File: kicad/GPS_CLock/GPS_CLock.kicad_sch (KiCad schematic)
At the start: 40 parts, among them J101 SWD, J102 UART, SW101 BOOT_JMP, SW102 SW_Push, SW103 SW_Push, U101 W25Q16JVUXIQ, U102 VEML7700-TR, U103 RP2040, U104 MS8607

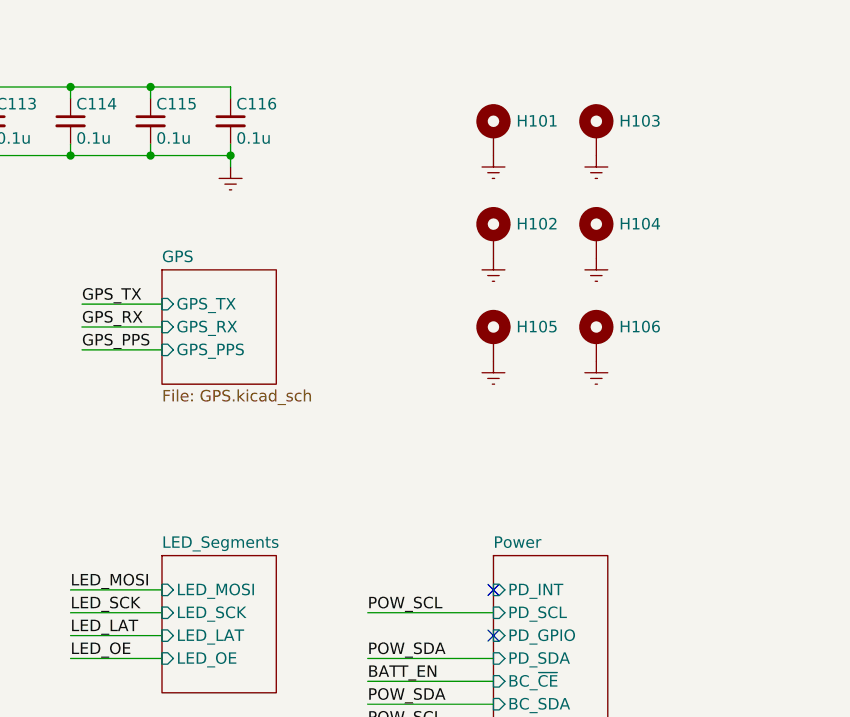
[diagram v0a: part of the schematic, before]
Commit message: change to larger segments
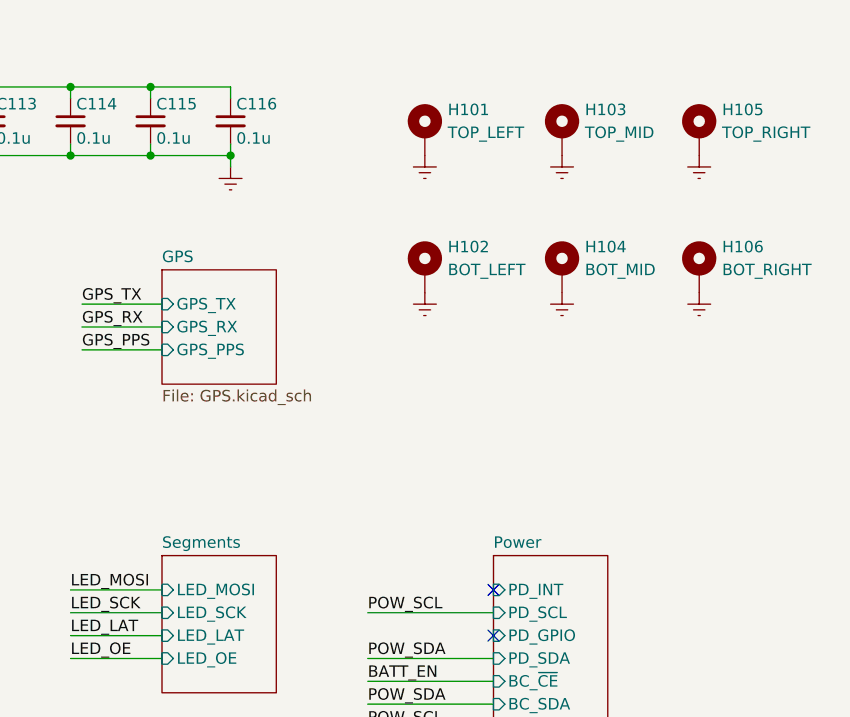
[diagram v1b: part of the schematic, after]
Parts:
- H101: value MountingHole_Pad -> TOP_LEFT; footprint MountingHole:MountingHole_2.2mm_M2_DIN965_Pad -> MountingHole:MountingHole_3.2mm_M3_DIN965_Pad
- H102: value MountingHole_Pad -> BOT_LEFT; footprint MountingHole:MountingHole_2.2mm_M2_DIN965_Pad -> MountingHole:MountingHole_3.2mm_M3_DIN965_Pad
- H103: value MountingHole_Pad -> TOP_MID; footprint MountingHole:MountingHole_2.2mm_M2_DIN965_Pad -> MountingHole:MountingHole_3.2mm_M3_DIN965_Pad
- H104: value MountingHole_Pad -> BOT_MID; footprint MountingHole:MountingHole_2.2mm_M2_DIN965_Pad -> MountingHole:MountingHole_3.2mm_M3_DIN965_Pad
- H105: value MountingHole_Pad -> TOP_RIGHT; footprint MountingHole:MountingHole_2.2mm_M2_DIN965_Pad -> MountingHole:MountingHole_3.2mm_M3_DIN965_Pad
- H106: value MountingHole_Pad -> BOT_RIGHT; footprint MountingHole:MountingHole_2.2mm_M2_DIN965_Pad -> MountingHole:MountingHole_3.2mm_M3_DIN965_Pad
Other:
- sheet LED_Segments renamed Segments
- sheet Segments: file LED_Segments.kicad_sch -> Segments.kicad_sch

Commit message: updated pcb
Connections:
- net LED_LAT renamed SEG_LAT
- net LED_MOSI renamed SEG_MOSI
- net LED_OE renamed SEG_OE
- net LED_SCK renamed SEG_CLK
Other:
- sheet Segments ports: added SEG_CLK_MCU, SEG_LAT_MCU, SEG_OE_MCU, SEG_SOUT_MCU; removed LED_LAT, LED_MOSI, LED_OE, LED_SCK

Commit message: update pcb
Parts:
- removed C108: 220n, Capacitor_SMD:C_0402_1005Metric, symbol Device:C_Small
- removed U104: MS8607, clock:MS8607, symbol Clock:MS8607
- SW102, SW103: footprint clock:EVQP4xB3x -> Button_Switch_SMD:SW_SPST_EVQP2
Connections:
- net OLED_CS is gone; now on net BTN_UP: U103.36 (GPIO24)
- net OLED_D/C is gone; now on net SEN_SCL: U103.34 (GPIO22)
- net OLED_RST is gone; now on net SEN_SDA: U103.35 (GPIO23)
- net BATT_EN: now also U103.37 (GPIO25); no longer U103.38 (GPIO26_ADC0)
- net BTN_DWN: now also U103.9 (GPIO7); no longer U103.28 (GPIO17)
- net BTN_UP: no longer U103.27 (GPIO16)
- net GPS_PPS: now also U103.28 (GPIO17); no longer U103.15 (GPIO12)
- net GPS_RX: now also U103.27 (GPIO16); no longer U103.14 (GPIO11)
- net GPS_TX: now also U103.18 (GPIO15); no longer U103.13 (GPIO10)
- net POW_SCL: now also U103.3 (GPIO1); no longer U103.39 (GPIO27_ADC1)
- net POW_SDA: now also U103.2 (GPIO0); no longer U103.40 (GPIO28_ADC2)
- net SEG_CLK: now also U103.14 (GPIO11); no longer U103.8 (GPIO6)
- net SEG_LAT: now also U103.13 (GPIO10); no longer U103.7 (GPIO5)
- net SEG_MOSI: now also U103.12 (GPIO9); no longer U103.6 (GPIO4)
- net SEG_OE: now also U103.15 (GPIO12); no longer U103.9 (GPIO7)
- net SEN_SCL: no longer U103.29 (GPIO18)
- net SEN_SDA: no longer U103.30 (GPIO19)
- net at J102.1 (Pin_1): now also U103.17 (GPIO14); no longer U103.12 (GPIO9)
- net at J102.2 (Pin_2): now also U103.16 (GPIO13); no longer U103.11 (GPIO8)
- net DISP_CS: now reaches U103.4 (GPIO2)
- net DISP_RST: now reaches U103.5 (GPIO3)
- net OLED_MOSI: no longer names the net of U103.31 (GPIO20)
- net OLED_SCK: no longer names the net of U103.32 (GPIO21)
- new net BC_INT: U103.39 (GPIO27_ADC1)
- new net DISP_BL: U103.11 (GPIO8)
- new net DISP_CLK: U103.7 (GPIO5)
- new net DISP_COPI: U103.8 (GPIO6)
- new net DISP_DC: U103.6 (GPIO4)
- new net SEG_2.5V_BOT_EN: U103.40 (GPIO28_ADC2)
- new net SEG_2.5V_TOP_EN: U103.38 (GPIO26_ADC0)
- no-connect marks 12 -> 2
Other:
- sheet Display ports: added DISP_BL, DISP_CLK, DISP_COPI, DISP_CS, DISP_DC, DISP_RST; removed OLED_CS, OLED_D/C, OLED_MOSI, OLED_RST, OLED_SCK
- sheet Power ports: added SEG_2.5V_BOT_EN, SEG_2.5V_TOP_EN; removed none
- moved on the sheet: J102

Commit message: update pcb
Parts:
- removed J101: SWD, Connector_PinHeader_1.27mm:PinHeader_1x03_P1.27mm_Vertical, symbol Connector_Generic:Conn_01x03
- removed J102: UART, Connector_PinHeader_1.27mm:PinHeader_1x02_P1.27mm_Vertical, symbol Connector_Generic:Conn_01x02
- added J101: Conn_01x07, Connector_PinHeader_1.27mm:PinHeader_1x07_P1.27mm_Vertical, symbol Connector_Generic:Conn_01x07
- added SW104: RUN, Button_Switch_SMD:SW_SPST_EVQP2, symbol Switch:SW_Push
- SW101: footprint clock:EVQP4xB3x -> Button_Switch_SMD:SW_SPST_EVQP2
- SW102: value SW_Push -> BTN_UP
- SW103: value SW_Push -> BTN_DWN
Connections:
- net +3V3: now also J101.1 (Pin_1)
- net Earth: now also J101.7 (Pin_7), SW104.2
- net GPS_PPS: now also U103.27 (GPIO16); no longer U103.28 (GPIO17)
- net GPS_RX: now also U103.28 (GPIO17); no longer U103.27 (GPIO16)
- net GPS_TX: now also U103.29 (GPIO18); no longer U103.18 (GPIO15)
- net RUN: now also J101.4 (Pin_4), SW104.1
- net SEG_CLK: now also U103.13 (GPIO10); no longer U103.14 (GPIO11)
- net SEG_LAT: now also U103.12 (GPIO9); no longer U103.13 (GPIO10)
- net SEG_MOSI: now also U103.14 (GPIO11); no longer U103.12 (GPIO9)
- net SWCLK: now also J101.6 (Pin_6)
- net SWD: now also J101.5 (Pin_5)
- net UART_RX: now reaches U103.30 (GPIO19)
- net UART_RX: now also J101.3 (Pin_3)
- net UART_TX: now reaches U103.31 (GPIO20)
- net UART_TX: now also J101.2 (Pin_2)

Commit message: update pcb
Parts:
- SW101, SW102, SW103, SW104: footprint Button_Switch_SMD:SW_SPST_EVQP2 -> clock:SW_SPST_EVQP2
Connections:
- net PD_INT: now also U103.16 (GPIO13)
- no-connect marks 2 -> 4
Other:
- sheet Power ports: added none; removed PD_GPIO

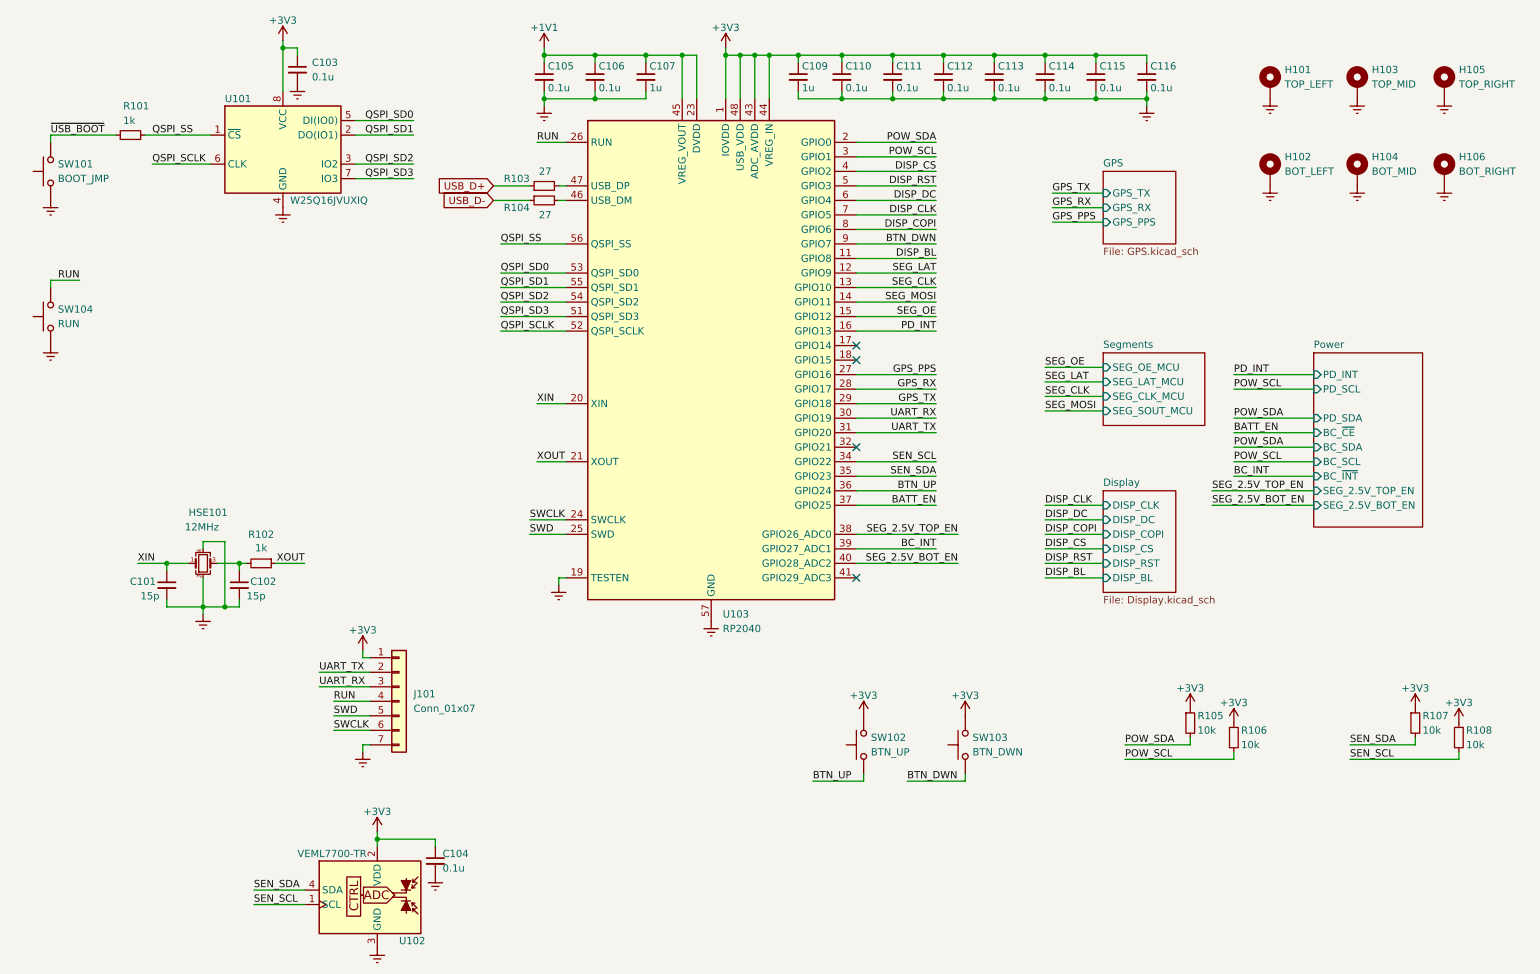
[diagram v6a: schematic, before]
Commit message: add quickcharge 3.0 capability
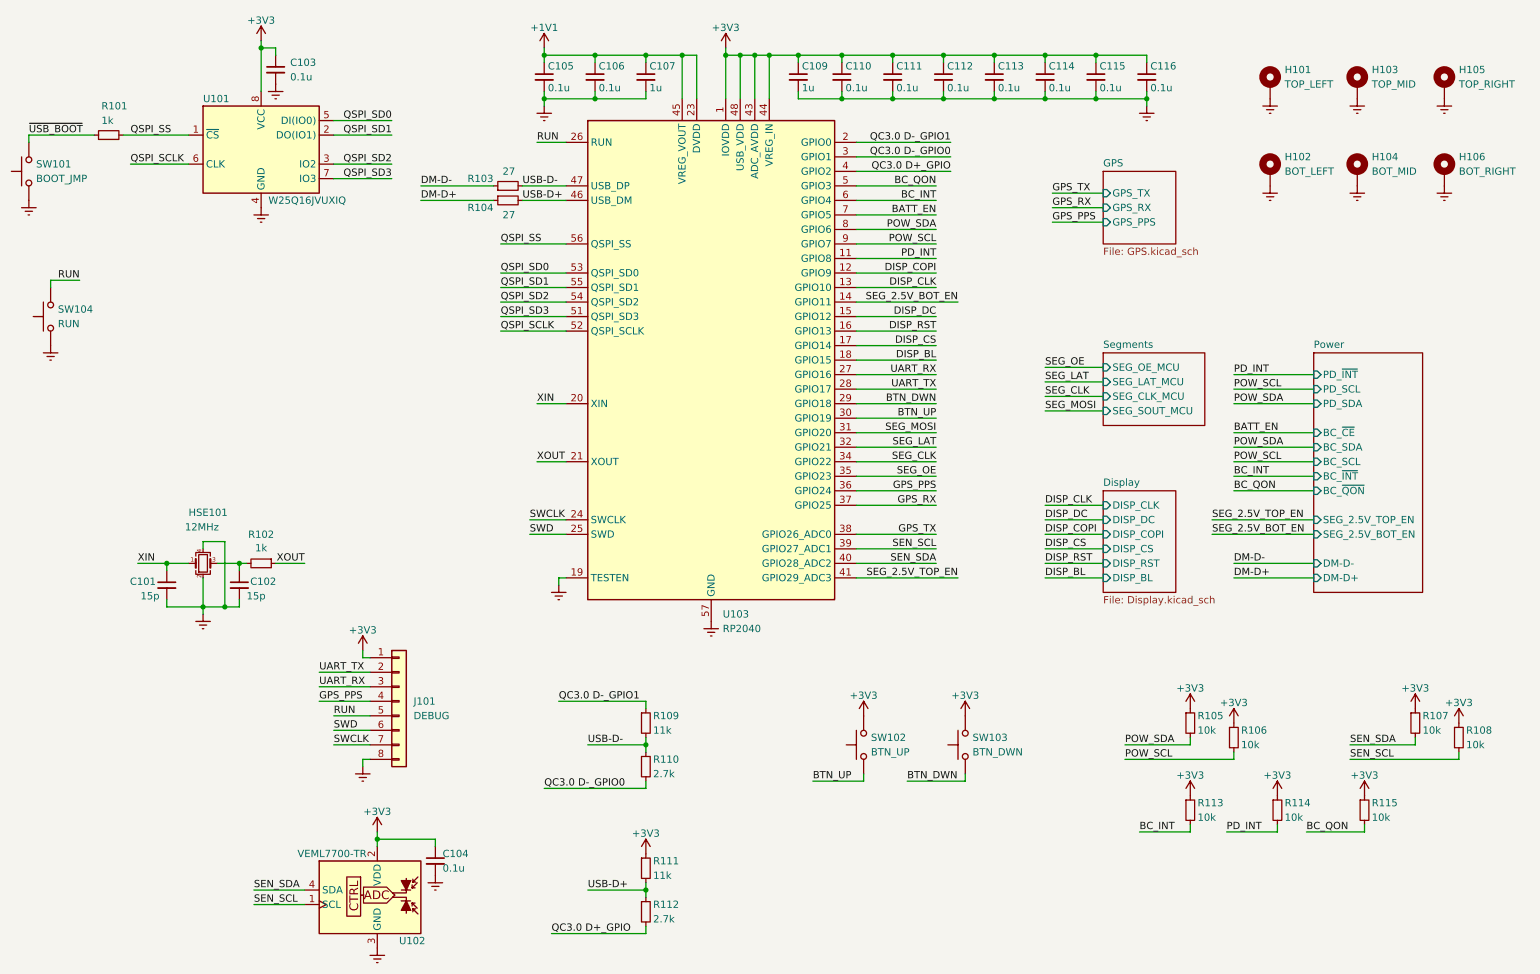
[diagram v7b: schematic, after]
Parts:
- added R109, R111: 11k, Resistor_SMD:R_0402_1005Metric, symbol Device:R_Small
- added R110, R112: 2.7k, Resistor_SMD:R_0402_1005Metric, symbol Device:R_Small
- added R113, R114, R115: 10k, Resistor_SMD:R_0402_1005Metric, symbol Device:R_Small
- J101: value Conn_01x07 -> DEBUG; footprint Connector_PinHeader_1.27mm:PinHeader_1x07_P1.27mm_Vertical -> Connector_PinHeader_1.27mm:PinHeader_1x08_P1.27mm_Vertical; symbol Connector_Generic:Conn_01x07 -> Connector_Generic:Conn_01x08
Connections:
- net +3V3: now also R111.1, R113.1, R114.1, R115.1
- net BATT_EN: now also U103.7 (GPIO5); no longer U103.37 (GPIO25)
- net BC_INT: now also U103.6 (GPIO4), R113.2; no longer U103.39 (GPIO27_ADC1)
- net BTN_DWN: now also U103.29 (GPIO18); no longer U103.9 (GPIO7)
- net BTN_UP: now also U103.30 (GPIO19); no longer U103.36 (GPIO24)
- net DISP_BL: now also U103.18 (GPIO15); no longer U103.11 (GPIO8)
- net DISP_CLK: now also U103.13 (GPIO10); no longer U103.7 (GPIO5)
- net DISP_COPI: now also U103.12 (GPIO9); no longer U103.8 (GPIO6)
- net DISP_CS: now also U103.17 (GPIO14); no longer U103.4 (GPIO2)
- net DISP_DC: now also U103.15 (GPIO12); no longer U103.6 (GPIO4)
- net DISP_RST: now also U103.16 (GPIO13); no longer U103.5 (GPIO3)
- net Earth: now also J101.8 (Pin_8); no longer J101.7 (Pin_7)
- net GPS_PPS: now also J101.4 (Pin_4), U103.36 (GPIO24); no longer U103.27 (GPIO16)
- net GPS_RX: now also U103.37 (GPIO25); no longer U103.28 (GPIO17)
- net GPS_TX: now also U103.38 (GPIO26_ADC0); no longer U103.29 (GPIO18)
- net PD_INT: now also U103.11 (GPIO8), R114.2; no longer U103.16 (GPIO13)
- net POW_SCL: now also U103.9 (GPIO7); no longer U103.3 (GPIO1)
- net POW_SDA: now also U103.8 (GPIO6); no longer U103.2 (GPIO0)
- net RUN: now also J101.5 (Pin_5); no longer J101.4 (Pin_4)
- net SEG_2.5V_BOT_EN: now also U103.14 (GPIO11); no longer U103.40 (GPIO28_ADC2)
- net SEG_2.5V_TOP_EN: now also U103.41 (GPIO29_ADC3); no longer U103.38 (GPIO26_ADC0)
- net SEG_CLK: now also U103.34 (GPIO22); no longer U103.13 (GPIO10)
- net SEG_LAT: now also U103.32 (GPIO21); no longer U103.12 (GPIO9)
- net SEG_MOSI: now also U103.31 (GPIO20); no longer U103.14 (GPIO11)
- net SEG_OE: now also U103.35 (GPIO23); no longer U103.15 (GPIO12)
- net SEN_SCL: now also U103.39 (GPIO27_ADC1); no longer U103.34 (GPIO22)
- net SEN_SDA: now also U103.40 (GPIO28_ADC2); no longer U103.35 (GPIO23)
- net SWCLK: now also J101.7 (Pin_7); no longer J101.6 (Pin_6)
- net SWD: now also J101.6 (Pin_6); no longer J101.5 (Pin_5)
- net UART_RX: now also U103.27 (GPIO16); no longer U103.30 (GPIO19)
- net UART_TX: now also U103.28 (GPIO17); no longer U103.31 (GPIO20)
- net USB-D-: now reaches R103.2, U103.47 (USB_DP)
- net USB-D-: now also R109.2, R110.1
- net USB-D+: now reaches R104.2, U103.46 (USB_DM)
- net USB-D+: now also R111.2, R112.1
- net USB_D+ renamed DM-D-
- net USB_D- renamed DM-D+
- new net BC_QON: R115.2, U103.5 (GPIO3)
- new net QC3.0 D+_GPIO: R112.2, U103.4 (GPIO2)
- new net QC3.0 D-_GPIO0: R110.2, U103.3 (GPIO1)
- new net QC3.0 D-_GPIO1: R109.1, U103.2 (GPIO0)
- no-connect marks 4 -> 0
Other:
- sheet Power ports: added BC_~{QON}, DM-D+, DM-D-, PD_~{INT}; removed PD_INT
- moved on the sheet: C103, R101, R103, R104, SW101, U101
